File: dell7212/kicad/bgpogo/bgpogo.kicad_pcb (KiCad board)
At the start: 2 copper layers, 76.7 x 72.2 mm, 10 parts, among them J1 Conn_02x13_Odd_Even, J2 USB1135-15-9-L-B_REVA1, J3 Conn_01x13, J4 PJ-019, J5 Conn_01x03, J6 Conn_01x13, J7 Conn_01x09, U1 AZ1117-5.0

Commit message: board v.9
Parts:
- added H1: MountingHole, MountingHole:MountingHole_2.5mm, F.Cu at (81.9, 34.0)
- added H2: MountingHole, MountingHole:MountingHole_2.5mm, F.Cu at (136.9, 34.0)
- added H3: MountingHole, MountingHole:MountingHole_2.5mm, F.Cu at (136.9, 124.0)
- added H4: MountingHole, MountingHole:MountingHole_2.5mm, F.Cu at (81.9, 124.0)
- moved U1 21.1 mm to (113.7, 108.3), turned to -90 degrees
- moved C2 16.9 mm to (115.8, 98.4)
- moved C1 9.10 mm to (109.7, 98.4), turned to 180 degrees
- moved J6 5.86 mm to (106.7, 59.5)
- moved J1 5.86 mm to (92.9, 55.6)
- moved J3 3.46 mm to (87.2, 62.6)
- moved J4 2.05 mm to (138.9, 53.0)
- moved J5 1.93 mm to (132.8, 61.7)
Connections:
- J7 pad 1: +5V -> /55
- J7 pad 2: /54 -> +5V
- J7 pad 3: /53 -> /56
- J7 pad 4: GND -> /54
- J7 pad 6: /59 -> /53
- J7 pad 8: /56 -> GND
- J7 pad 9: /55 -> /59
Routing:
- net /55: track 0.00 -> 48.1 mm
- net +8V: track 0.00 -> 47.2 mm
- net /54: track 0.00 -> 44.6 mm
- net /53: track 0.00 -> 41.6 mm
- net +5V: track 0.00 -> 40.6 mm
- net /59: track 0.00 -> 39.6 mm
- net /56: track 0.00 -> 39.5 mm
- net /58: track 0.00 -> 38.4 mm, vias 0 -> 2
- net GND: track 0.00 -> 20.1 mm
- net Net-(J5-Pin_2): track 0.00 -> 13.0 mm
- net +3.3V: track 0.00 -> 11.2 mm
- net /p1: track 0.00 -> 11.2 mm
- net /p21: track 0.00 -> 10.5 mm
- net /p3: track 0.00 -> 10.1 mm
- net /p19: track 0.00 -> 9.95 mm
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- added copper zone on B.Cu, net GND
- added copper zone on F.Cu, net GND
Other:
- board size 76.7 x 72.2 mm -> 69.4 x 99.5 mm

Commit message: board v1.0 ordered
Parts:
- added J8: PJ-104H, PJ_104H:SAMESKY_PJ-104H, F.Cu at (139.9, 105.1)
- added J9: Conn_01x03, Connector_PinHeader_2.54mm:PinHeader_1x03_P2.54mm_Vertical, F.Cu at (131.8, 94.0)
- moved J1 23.8 mm to (94.9, 79.3)
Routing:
- net Net-(J9-Pin_2): track 0.00 -> 13.4 mm
- net Net-(J9-Pin_1): track 0.00 -> 10.0 mm
- net Net-(J9-Pin_3): track 0.00 -> 7.57 mm
- net /54: track 44.6 -> 42.5 mm
- net /53: track 41.6 -> 39.8 mm
- net /p1: track 11.2 -> 10.1 mm
- net +8V: track 47.2 -> 46.2 mm
- net /56: track 39.5 -> 38.7 mm
- net /p2: track 9.51 -> 8.90 mm
- net /p4: track 8.94 -> 8.40 mm
- net /p3: track 10.1 -> 9.57 mm
- net /55: track 48.1 -> 47.6 mm
- net +5V: track 40.6 -> 40.5 mm, vias 0 -> 20
- added copper zone on B.Cu, net +5V
- added copper zone on F.Cu, net +5V
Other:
- board text added: "DellPogo v1.0 github.com/CarlFK/geebee"

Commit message: unground the groungs
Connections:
- net +3.3V renamed /p23
- J1 pad 11: GND -> /p11
- J1 pad 12: GND -> /p12
- J1 pad 17: GND -> /p17
- J1 pad 18: GND -> /p18
- J1 pad 24: GND -> /p24
- J1 pad 25: +8V -> /p25
- J1 pad 26: +8V -> /p26
- J1 pad 5: GND -> /p5
- J1 pad 6: GND -> /p6
- J3 pad 13: +8V -> /p25
- J3 pad 3: GND -> /p5
- J3 pad 6: GND -> /p11
- J3 pad 9: GND -> /p17
- J6 pad 12: GND -> /p24
- J6 pad 13: +8V -> /p26
- J6 pad 3: GND -> /p6
- J6 pad 6: GND -> /p12
- J6 pad 9: GND -> /p18
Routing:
- net +8V: track 46.2 -> 30.2 mm
- net /p24: track 0.00 -> 13.8 mm
- net /p25: track 0.00 -> 12.0 mm
- net /p18: track 0.00 -> 10.7 mm
- net /p17: track 0.00 -> 9.46 mm
- net /p12: track 0.00 -> 9.17 mm
- net /p5: track 0.00 -> 9.07 mm
- net /p6: track 0.00 -> 7.90 mm
- net /p11: track 0.00 -> 7.83 mm
- net /p23: track 10.8 -> 11.6 mm
- net /58: track 38.5 -> 38.2 mm, vias 2 -> 1
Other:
- board text added: "DellPogo v2.0 github.com/CarlFK/geebee"
- board text removed: "DellPogo v1.0 github.com/CarlFK/geebee"

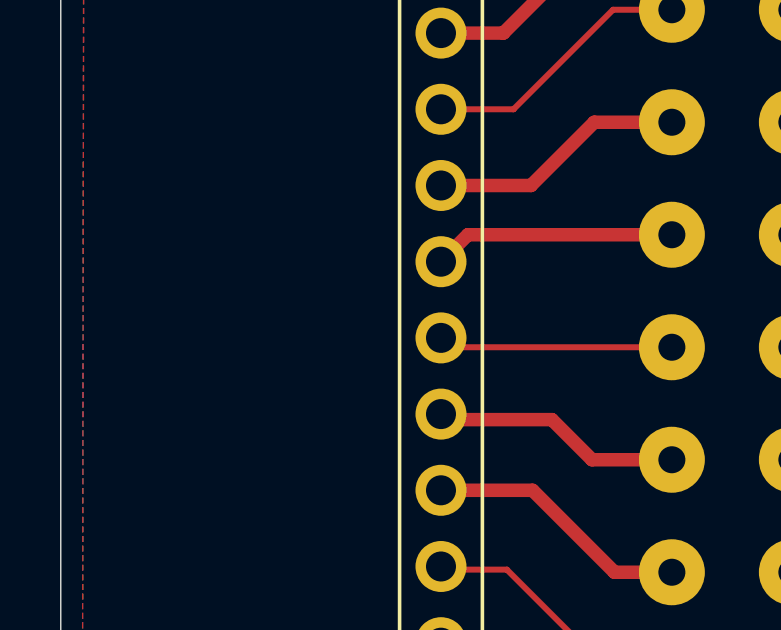
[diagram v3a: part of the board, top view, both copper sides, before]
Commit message: ground plane, gnd not connected (bad).
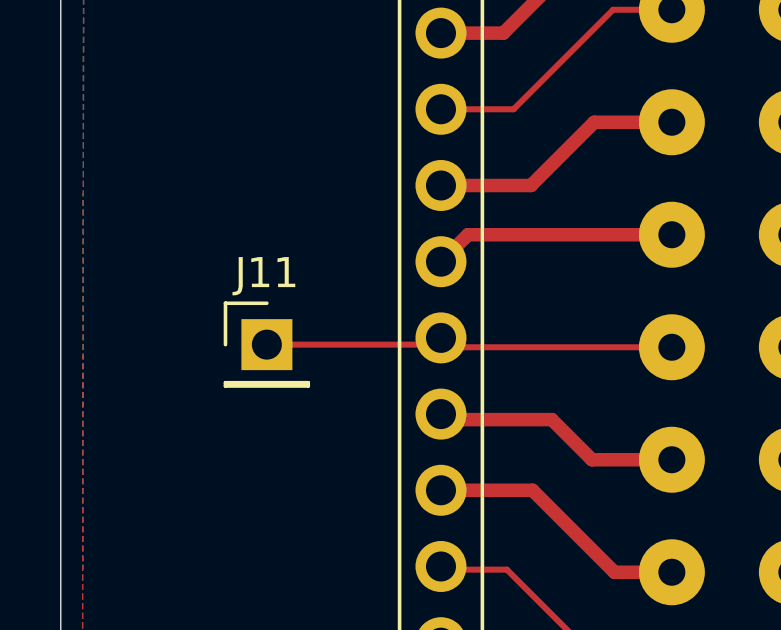
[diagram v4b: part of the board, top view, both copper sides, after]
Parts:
- added J11: Conn_01x01, Connector_PinHeader_2.54mm:PinHeader_1x01_P2.54mm_Vertical, F.Cu at (81.4, 75.5)
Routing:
- net /p11: track 7.83 -> 13.7 mm

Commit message: ground pogos connected to GND via solder bridge. and bigger traces.
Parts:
- removed J11: Conn_01x01, Connector_PinHeader_2.54mm:PinHeader_1x01_P2.54mm_Vertical
- added JP1: SolderJumper_2_Bridged, Jumper:SolderJumper-2_P1.3mm_Open_RoundedPad1.0x1.5mm, F.Cu at (83.4, 68.0)
- added JP2: SolderJumper_2_Bridged, Jumper:SolderJumper-2_P1.3mm_Bridged_RoundedPad1.0x1.5mm, F.Cu at (83.4, 75.5)
- added JP3: SolderJumper_2_Bridged, Jumper:SolderJumper-2_P1.3mm_Bridged_RoundedPad1.0x1.5mm, F.Cu at (83.4, 83.0)
- added JP4: SolderJumper_2_Bridged, Jumper:SolderJumper-2_P1.3mm_Bridged_RoundedPad1.0x1.5mm, F.Cu at (83.4, 90.5)
- added JP5: SolderJumper_2_Bridged, Jumper:SolderJumper-2_P1.3mm_Open_RoundedPad1.0x1.5mm, F.Cu at (110.6, 64.5)
- added JP6: SolderJumper_2_Bridged, Jumper:SolderJumper-2_P1.3mm_Bridged_RoundedPad1.0x1.5mm, F.Cu at (110.3, 72.0)
- added JP7: SolderJumper_2_Bridged, Jumper:SolderJumper-2_P1.3mm_Bridged_RoundedPad1.0x1.5mm, F.Cu at (110.6, 80.0)
- added JP8: SolderJumper_2_Bridged, Jumper:SolderJumper-2_P1.3mm_Bridged_RoundedPad1.0x1.5mm, F.Cu at (110.4, 87.5)
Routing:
- net +8V: track 30.2 -> 15.2 mm
- net /p26: track 0.00 -> 14.5 mm
- net /p18: track 10.7 -> 14.1 mm
- net /p5: track 9.07 -> 12.4 mm
- net /p6: track 7.90 -> 11.2 mm
- net /p17: track 9.46 -> 12.7 mm
- net /p23: track 11.6 -> 14.8 mm
- net /p24: track 13.8 -> 16.9 mm
- net /p12: track 9.17 -> 12.2 mm
- net /p11: track 13.7 -> 11.2 mm
- net /54: track 42.5 -> 41.9 mm
- net GND: vias 0 -> 6

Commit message: power nets, not really.
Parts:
- removed J4: PJ-019, libs:CUI_PJ-019
- removed J5: Conn_01x03, Connector_PinHeader_2.54mm:PinHeader_1x03_P2.54mm_Vertical
- moved J8 53.2 mm to (139.3, 51.9)
- moved J9 35.3 mm to (129.2, 58.8)
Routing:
- net Net-(J5-Pin_2): track 13.0 -> 0.00 mm
- net Net-(J5-Pin_1): track 8.91 -> 0.00 mm
- net Net-(J5-Pin_3): track 8.74 -> 0.00 mm
- net Net-(J9-Pin_2): track 13.4 -> 5.39 mm
- net Net-(J9-Pin_3): track 7.57 -> 10.9 mm
- net Net-(J9-Pin_1): track 10.0 -> 8.83 mm

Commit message: Power Now.
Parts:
- moved JP1 2.15 mm to (81.3, 68.0)
- moved JP5 2.02 mm to (111.9, 66.0)
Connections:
- J8 pad 1: Net-(J9-Pin_1) -> /p6
- J8 pad 2: Net-(J9-Pin_3) -> /p5
- J9 pad 1: Net-(J9-Pin_1) -> /p6
- J9 pad 3: Net-(J9-Pin_3) -> /p5
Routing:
- net /p5: track 12.4 -> 103.0 mm
- net /p6: track 11.2 -> 49.1 mm
- net Net-(J9-Pin_3): track 10.9 -> 0.00 mm
- net Net-(J9-Pin_1): track 8.83 -> 0.00 mm
